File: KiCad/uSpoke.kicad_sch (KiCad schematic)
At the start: 67 parts, among them J12 Amphenol 132289, J2 PLS-1x3, J4 PLS-1x3, Q2 AO3407A, Q3 AO3400, Q5 AO3400, U1 SP0503BAHTG, U2 TP4056, U4 LM3671MF-3.3, U5 74HC4052PW, U6 STM32F103C8T6, X1 8MHz

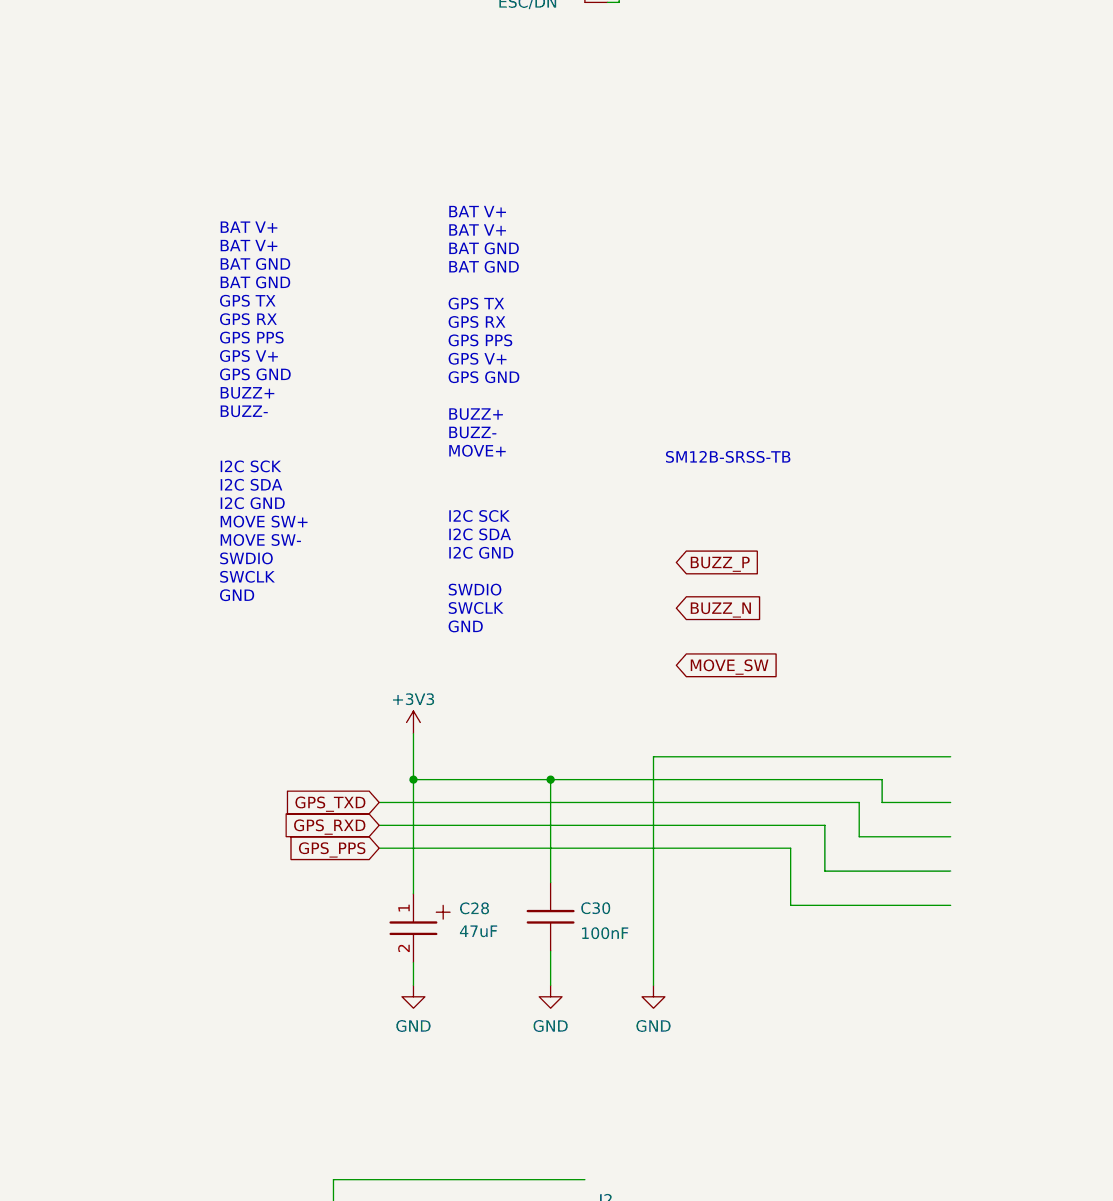
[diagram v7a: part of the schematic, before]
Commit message: Add 12P connector
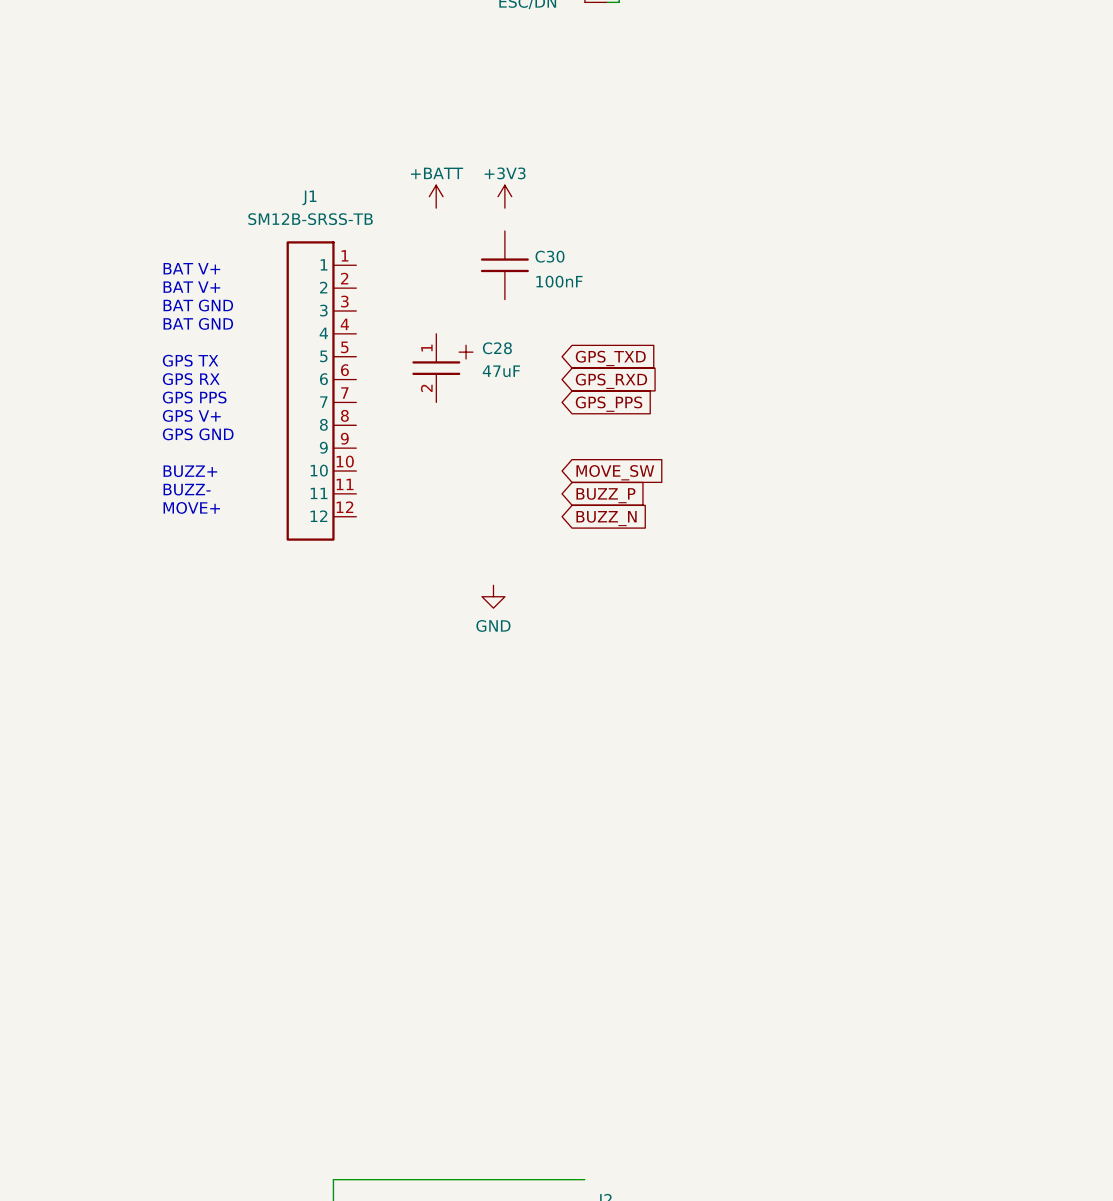
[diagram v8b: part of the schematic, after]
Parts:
- added J1: SM12B-SRSS-TB, symbol uSpoke:SM12B-SRSS-TB
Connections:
- net +3V3: no longer C28.1, C30.1
- net GND: no longer C28.2, C30.2
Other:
- note removed: "BAT V+ BAT V+ BAT GND BAT GND GPS TX GPS RX GPS PPS GPS V+ GPS GND BUZZ+ BUZZ- I2C SCK I2C SDA I2C GND MOVE SW+ MOVE SW- SWDIO SWCLK GND"
- note removed: "I2C SCK I2C SDA I2C GND SWDIO SWCLK GND"
- note removed: "SM12B-SRSS-TB"
- moved on the sheet: C28, C30
